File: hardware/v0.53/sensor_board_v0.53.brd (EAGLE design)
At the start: 56.4 x 41.7 mm, 58 parts, among them J3 USB-MICROB, J6 AVR_SPI_PRG_6PTH, U1 ATMEGA328P, U10 TSL2591, U3 OPA344, U4 RFM69HW, U5 FT231XS, U6 ADMP401, U8 MCP1703CB, U9 BMP280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

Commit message: Fixed attributes
Updated MPN for 1K ohm resistor
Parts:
- R14, R4: value 10K -> 1K
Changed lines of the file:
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@@
 <attribute name="VALUE" x="7.1882" y="30.3784" size="1.27" layer="27" rot="R90"/>
 </element>
-<element name="R4" library="SparkFun-Passives" package="0805" value="10K" x="12.0904" y="45.212" smashed="yes">
-<attribute name="MPN" value="RC0805FR-0710KL" x="12.0904" y="45.212" size="1.778" layer="27" display="off"/>
+<element name="R4" library="SparkFun-Passives" package="0805" value="1K" x="12.0904" y="45.212" smashed="yes">
+<attribute name="MPN" value="RC0805FR-071KL" x="12.0904" y="45.212" size="1.778" layer="27" display="off"/>
 <attribute name="NAME" x="11.6332" y="46.1391" size="0.6096" layer="121" font="vector"/>
 </element>
-<element name="R14" library="SparkFun-Passives" package="0805" value="10K" x="23.4696" y="35.814" smashed="yes" rot="R180">
-<attribute name="MPN" value="RC0805FR-0710KL" x="23.4696" y="35.814" size="1.778" layer="27" rot="R180" display="off"/>
+<element name="R14" library="SparkFun-Passives" package="0805" value="1K" x="23.4696" y="35.814" smashed="yes" rot="R180">
+<attribute name="MPN" value="RC0805FR-071KL" x="23.4696" y="35.814" size="1.778" layer="27" rot="R180" display="off"/>
 <attribute name="NAME" x="24.7396" y="36.6903" size="0.6096" layer="121" font="vector" align="bottom-center"/>
 </element>

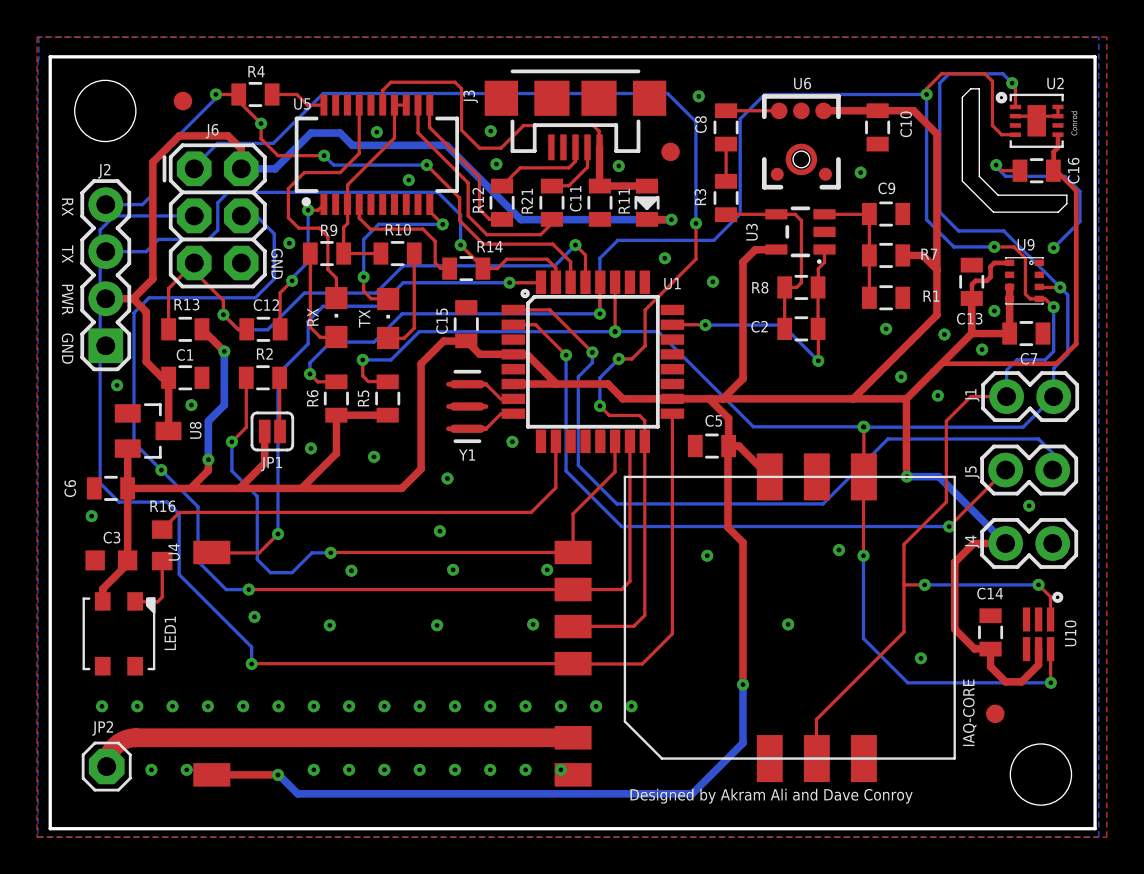
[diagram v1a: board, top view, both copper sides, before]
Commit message: Via and keepout adjustments
and silkscreen adjustments
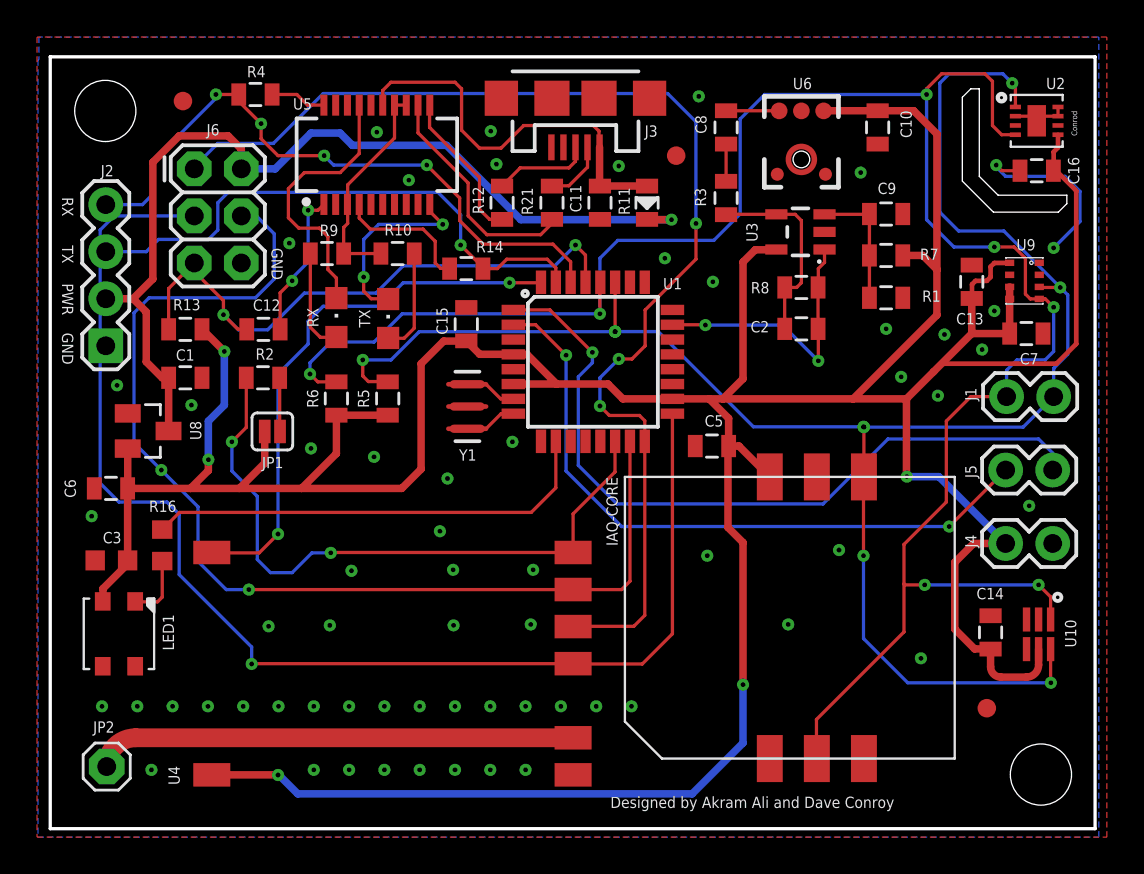
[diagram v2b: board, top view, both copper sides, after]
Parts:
- moved U$2 0.55 mm to (51.6, 12.1)
- moved U$3 0.37 mm to (34.8, 41.9)
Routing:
- net GND: vias 65 -> 63
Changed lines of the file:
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@@
 <setting verticaltext="up"/>
 </settings>
-<grid distance="5" unitdist="mil" unit="mil" style="lines" multiple="1" display="yes" altdistance="0.01" altunitdist="inch" altunit="inch"/>
+<grid distance="2" unitdist="mil" unit="mil" style="lines" multiple="1" display="yes" altdistance="0.01" altunitdist="inch" altunit="inch"/>
 <layers>
 <layer number="1" name="Top" color="4" fill="1" visible="yes" active="yes"/>
@@
 <plain>
 <text x="36.6268" y="10.9728" size="1.016" layer="122" font="vector" ratio="16" rot="MR0" align="center-left">Touchstone</text>
-<text x="32.258" y="7.112" size="0.6096" layer="121" font="vector">Designed by Akram Ali and Dave Conroy</text>
+<text x="31.242" y="6.7056" size="0.6096" layer="121" font="vector">Designed by Akram Ali and Dave Conroy</text>
 <text x="36.5506" y="9.525" size="0.6096" layer="122" font="vector" rot="MR0">v0.53 | March 2017</text>
 <text x="3.5052" y="20.6756" size="0.8128" layer="122" font="vector" ratio="12" rot="MR270">crtlabs.org</text>
@@
 <attribute name="MF" value="" x="32.0294" y="9.3726" size="1.778" layer="27" rot="R90" display="off"/>
 <attribute name="MPN" value="IAQ-CORE C" x="32.0294" y="9.3726" size="1.778" layer="27" rot="R90" display="off"/>
-<attribute name="NAME" x="50.2854" y="13.6906" size="0.6096" layer="121" font="vector" rot="R270"/>
+<attribute name="NAME" x="31.0322" y="24.5618" size="0.6096" layer="121" font="vector" rot="R270"/>
 </element>
 <element name="U1" library="SparkFun-DigitalIC" package="TQFP32-08" value="ATMEGA328P" x="30.3022" y="30.7848" smashed="yes">
@@
 <element name="J3" library="SparkFun-Connectors" package="USB-MICROB" value="USB-MICROB" x="29.3624" y="45.0088" smashed="yes" rot="R180">
 <attribute name="PROD_ID" value="CONN-09505" x="29.3624" y="45.0088" size="1.778" layer="27" rot="R180" display="off"/>
-<attribute name="NAME" x="23.3228" y="45.4912" size="0.6096" layer="121" font="vector" rot="R270"/>
+<attribute name="NAME" x="33.0964" y="42.9316" size="0.6096" layer="121" font="vector"/>
 <attribute name="MPN" value="47346-0001" x="29.3624" y="45.0088" size="1.778" layer="27" rot="R180" display="off"/>
 </element>
@@
 </element>
 <element name="U4" library="RFM69 USB Gateway" package="LOWPOWERLAB_RFM69W-MINPADS" value="RFM69HW" x="21.2344" y="15.494" smashed="yes">
-<attribute name="NAME" x="8.0048" y="19.9856" size="0.6096" layer="121" font="vector" rot="R90"/>
+<attribute name="NAME" x="8.0048" y="7.946" size="0.6096" layer="121" font="vector" rot="R90"/>
 <attribute name="MPN" value="RFM69HW" x="21.2344" y="15.494" size="1.778" layer="27" display="off"/>
 </element>
@@
 </element>
 <element name="U$1" library="adafruit" package="FIDUCIAL_1MM" value="FIDUCIAL" x="8.1788" y="44.8564"/>
-<element name="U$2" library="adafruit" package="FIDUCIAL_1MM" value="FIDUCIAL" x="52.0192" y="11.7856"/>
-<element name="U$3" library="adafruit" package="FIDUCIAL_1MM" value="FIDUCIAL" x="34.4932" y="42.1132"/>
+<element name="U$2" library="adafruit" package="FIDUCIAL_1MM" value="FIDUCIAL" x="51.562" y="12.0904"/>
+<element name="U$3" library="adafruit" package="FIDUCIAL_1MM" value="FIDUCIAL" x="34.798" y="41.91"/>
 <element name="U10" library="TSL2591" package="DFN6_TAOS" value="TSL2591" x="54.356" y="16.0782" smashed="yes" rot="R270">
 <attribute name="NAME" x="56.3896" y="15.367" size="0.6096" layer="121" font="vector" rot="R90"/>
@@
 </element>
 <element name="LED1" library="adafruit" package="LED3535" value="WS2812B3535" x="4.7244" y="16.1036" smashed="yes" rot="R270">
-<attribute name="NAME" x="7.1882" y="16.129" size="0.6096" layer="121" font="vector" rot="R270" align="bottom-center"/>
+<attribute name="NAME" x="7.0866" y="16.1798" size="0.6096" layer="121" font="vector" rot="R270" align="bottom-center"/>
 <attribute name="MPN" value="SK6812 mini" x="4.7244" y="16.1036" size="1.778" layer="27" rot="R270" display="off"/>
 </element>
@@
 <element name="J2" library="SparkFun-Connectors" package="1X04" value="" x="4.0132" y="31.6484" smashed="yes" rot="R90">
 <attribute name="PROD_ID" value="CONN-09696" x="4.0132" y="31.6484" size="1.778" layer="27" rot="R90" display="off"/>
-<attribute name="NAME" x="3.9878" y="41.4528" size="0.6096" layer="121" font="vector" rot="R180" align="bottom-center"/>
+<attribute name="NAME" x="4.0894" y="41.402" size="0.6096" layer="121" font="vector" rot="R180" align="bottom-center"/>
 <attribute name="VALUE" x="7.1882" y="30.3784" size="1.27" layer="27" rot="R90"/>
 </element>
@@
 <via x="11.43" y="12.192" extent="1-16" drill="0.254" diameter="0.127"/>
 <via x="9.525" y="12.192" extent="1-16" drill="0.254" diameter="0.127"/>
-<via x="28.575" y="8.763" extent="1-16" drill="0.254" diameter="0.127"/>
 <via x="26.67" y="8.763" extent="1-16" drill="0.254" diameter="0.127"/>
 <via x="24.765" y="8.763" extent="1-16" drill="0.254" diameter="0.127"/>
@@
 <via x="22.0472" y="21.6408" extent="1-16" drill="0.254" diameter="0.127"/>
 <via x="36.7792" y="35.1028" extent="1-16" drill="0.254" diameter="0.127"/>
-<via x="27.0764" y="16.6116" extent="1-16" drill="0.254" diameter="0.127"/>
-<via x="21.8948" y="16.5608" extent="1-16" drill="0.254" diameter="0.127"/>
+<via x="26.9494" y="16.6116" extent="1-16" drill="0.254" diameter="0.127"/>
+<via x="22.7838" y="16.5608" extent="1-16" drill="0.254" diameter="0.127"/>
 <via x="16.1036" y="16.5608" extent="1-16" drill="0.254" diameter="0.127"/>
-<via x="12.0396" y="17.018" extent="1-16" drill="0.254" diameter="0.127"/>
-<via x="27.8384" y="19.558" extent="1-16" drill="0.254" diameter="0.127"/>
+<via x="12.8016" y="16.51" extent="1-16" drill="0.254" diameter="0.127"/>
+<via x="27.0764" y="19.558" extent="1-16" drill="0.254" diameter="0.127"/>
 <via x="22.7584" y="19.558" extent="1-16" drill="0.254" diameter="0.127"/>
 <via x="4.6228" y="29.5148" extent="1-16" drill="0.254" diameter="0.127"/>
@@
 <via x="5.715" y="12.192" extent="1-16" drill="0.254" diameter="0.127"/>
 <via x="3.81" y="12.192" extent="1-16" drill="0.254" diameter="0.127"/>
-<via x="8.382" y="8.763" extent="1-16" drill="0.254" diameter="0.127"/>
 <via x="6.477" y="8.763" extent="1-16" drill="0.254" diameter="0.127"/>
 <via x="51.9684" y="33.528" extent="1-16" drill="0.254" diameter="0.127"/>
@@
 <wire x1="51.7542" y1="15.2908" x2="51.7652" y2="15.2798" width="0.4064" layer="1"/>
 <wire x1="54.356" y1="15.2782" x2="54.356" y2="14.4272" width="0.4064" layer="1"/>
-<wire x1="54.356" y1="14.4272" x2="53.4416" y2="13.5128" width="0.4064" layer="1"/>
-<wire x1="53.4416" y1="13.5128" x2="52.578" y2="13.5128" width="0.4064" layer="1"/>
-<wire x1="52.578" y1="13.5128" x2="51.7652" y2="14.3256" width="0.4064" layer="1"/>
 <wire x1="51.7652" y1="14.3256" x2="51.7652" y2="15.2798" width="0.4064" layer="1"/>
 <wire x1="14.5796" y1="23.9522" x2="11.2268" y2="23.9522" width="0.4064" layer="1"/>
@@
 <wire x1="26.0032" y1="31.1912" x2="24.1952" y2="31.1912" width="0.4064" layer="1"/>
 <wire x1="24.1952" y1="31.1912" x2="23.4696" y2="31.9168" width="0.4064" layer="1"/>
+<wire x1="51.7652" y1="14.3256" x2="52.324" y2="13.7668" width="0.4064" layer="1" curve="90"/>
+<wire x1="52.324" y1="13.7668" x2="53.6956" y2="13.7668" width="0.4064" layer="1"/>
+<wire x1="53.6956" y1="13.7668" x2="54.356" y2="14.4272" width="0.4064" layer="1" curve="90"/>
 </signal>
 <signal name="SCL">
